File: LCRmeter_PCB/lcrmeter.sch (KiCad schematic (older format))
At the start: 63 parts, among them J1 LCR_input, J2 LCR_input, J3 Conn_01x06, J4 USB_B_Micro, J5 OSCILLOSCOPE, J6 misc, J7 misc, SW1 power, SW2 +, SW3 -, SW4 ok, SW5 back, U1 MCP47, U2 STM32F103C8Tx, U3 OLED, U4 74HC14, U5 MCP6001-OT, Y1 8Mhz

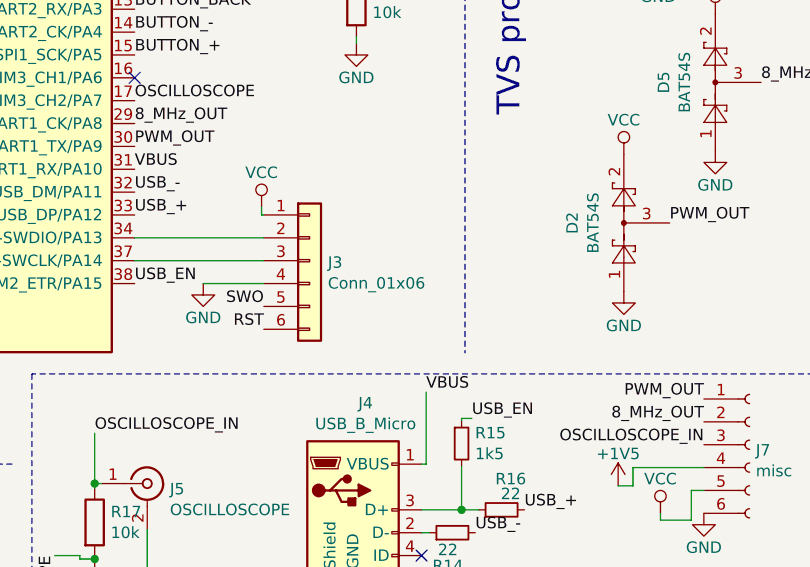
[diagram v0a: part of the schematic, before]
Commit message: added new i2c and dac classes
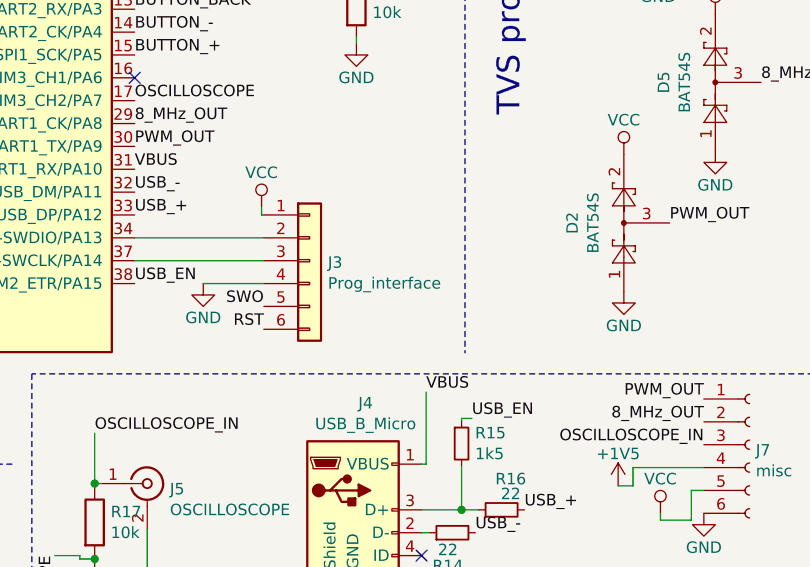
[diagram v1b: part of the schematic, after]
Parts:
- J3: value Conn_01x06 -> Prog_interface
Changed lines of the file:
@@
 P 8775 4220
 F 0 "J3" H 8855 4212 50  0000 L CNN
-F 1 "Conn_01x06" H 8855 4121 50  0000 L CNN
+F 1 "Prog_interface" H 8855 4121 50  0000 L CNN
 F 2 "Connector_PinHeader_2.54mm:PinHeader_1x06_P2.54mm_Vertical" H 8775 4220 50  0001 C CNN
 F 3 "~" H 8775 4220 50  0001 C CNN

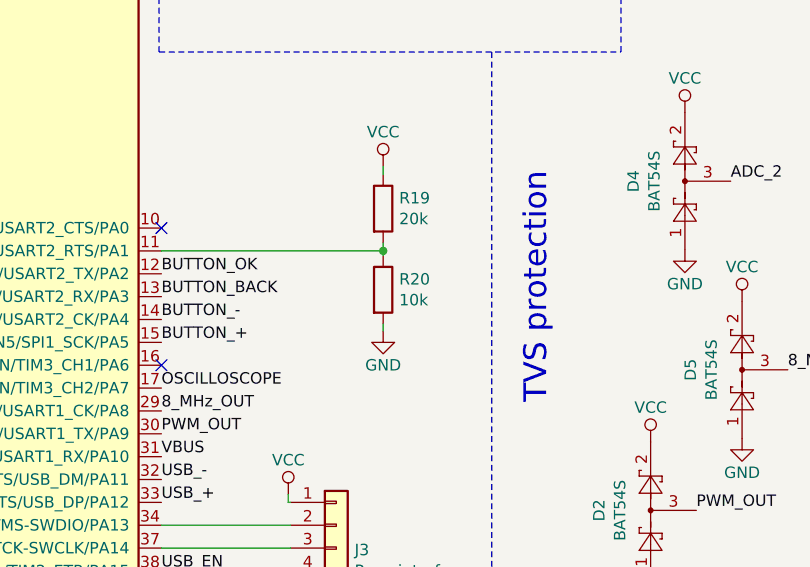
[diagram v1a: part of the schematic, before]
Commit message: fixed schematic- diode reference and minor problems
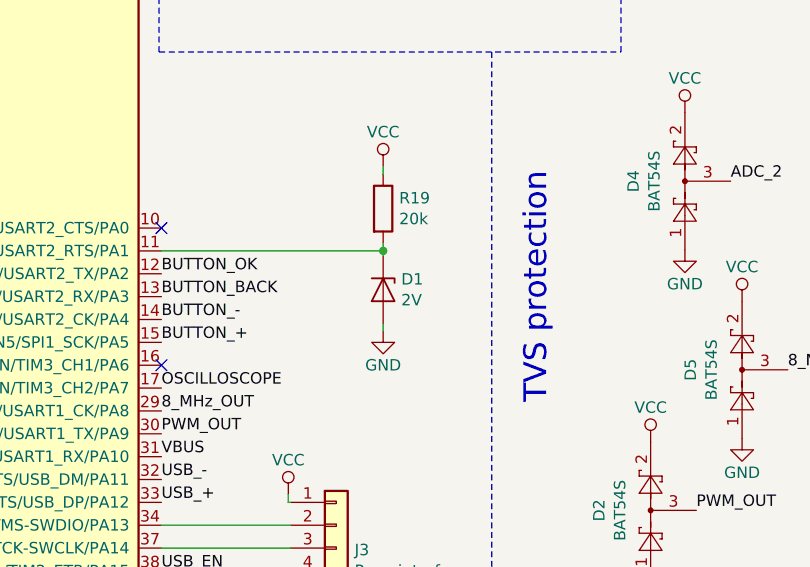
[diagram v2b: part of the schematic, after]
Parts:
- removed R20: 10k, Resistor_SMD:R_0603_1608Metric_Pad1.05x0.95mm_HandSolder, symbol Device:R
- added D1: 2V, Diode_SMD:D_MiniMELF, symbol Device:D_Zener
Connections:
- net GND: now also D1.2 (A)
- net at R19.2, U2.11 (ADC1_IN1/ADC2_IN1/TIM2_CH2/USART2_RTS/PA1): now also D1.1 (K)
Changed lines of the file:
@@
-	1    0    0    -1
-$EndComp
-$Comp
-L Device:R R20
-U 1 1 5C89377D
-P 8980 3090
-F 0 "R20" H 9050 3136 50  0000 L CNN
-F 1 "10k" H 9050 3045 50  0000 L CNN
-F 2 "Resistor_SMD:R_0603_1608Metric_Pad1.05x0.95mm_HandSolder" V 8910 3090 50  0001 C CNN
-F 3 "~" H 8980 3090 50  0001 C CNN
-	1    8980 3090
 	1    0    0    -1
 $EndComp
 Wire Wire Line
-	8980 2940 8980 2920
-Wire Wire Line
 	8010 2920 8980 2920
-Connection ~ 8980 2920
-Wire Wire Line
-	8980 2920 8980 2885
 $Comp
 L power:GND #PWR09
@@
 	7835 4975 7835 5195
 Connection ~ 7835 5195
+$Comp
+L Device:D_Zener D1
+U 1 1 5CFAB46B
+P 8980 3090
+F 0 "D1" V 8934 3169 50  0000 L CNN
+F 1 "2V" V 9025 3169 50  0000 L CNN
+F 2 "Diode_SMD:D_MiniMELF" H 8980 3090 50  0001 C CNN
+F 3 "~" H 8980 3090 50  0001 C CNN
+	1    8980 3090
+	0    1    1    0
+$EndComp
+Wire Wire Line
+	8980 2885 8980 2920
+Connection ~ 8980 2920
+Wire Wire Line
+	8980 2920 8980 2940
 $EndSCHEMATC
